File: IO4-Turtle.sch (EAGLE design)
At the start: 30 parts, among them CON1 RJ12/6, IC1 TC4428A, IC2 NE555S, Q1 NPN, X2 MSTBA5

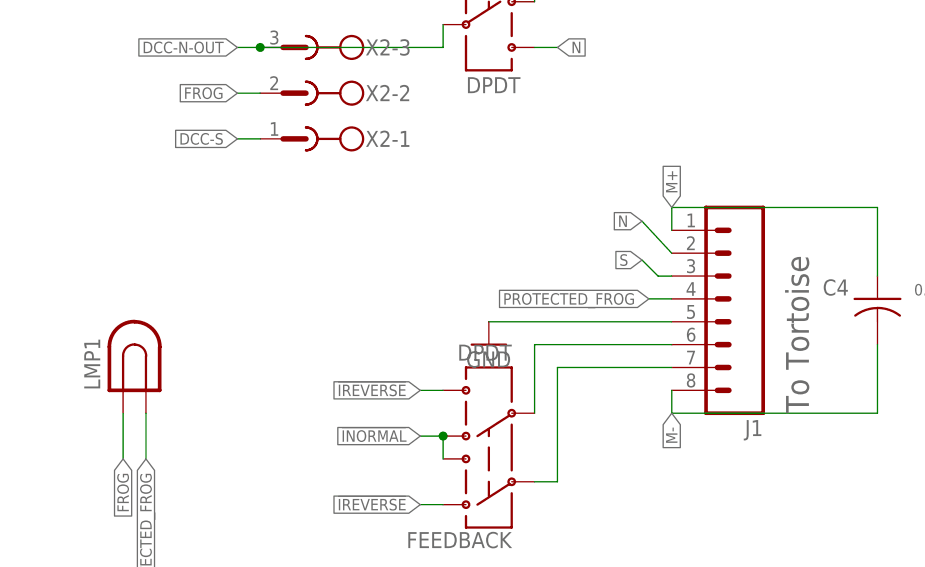
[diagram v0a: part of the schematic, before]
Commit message: added values for connectors
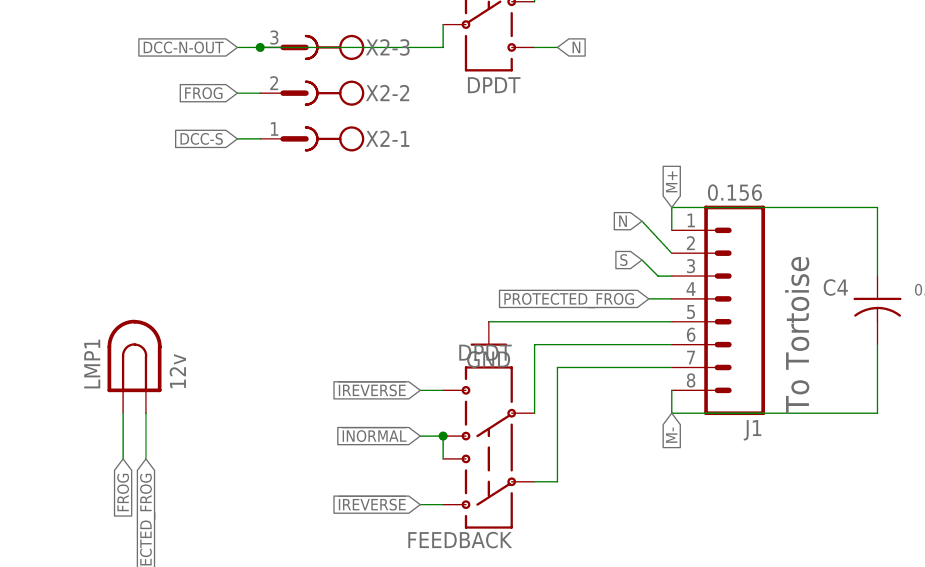
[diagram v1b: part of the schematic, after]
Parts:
- J1: value (none) -> 0.156
- LMP1: value (none) -> 12v
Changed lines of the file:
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@@
 <part name="P+4" library="SPCoast" deviceset="VCCIO" device=""/>
 <part name="P+5" library="SPCoast" deviceset="VCC" device=""/>
-<part name="LMP1" library="SPCoast" deviceset="LAMP" device="BULB"/>
-<part name="J1" library="SPCoast" deviceset="CONNECTOR-M08" device="1.56-F"/>
+<part name="LMP1" library="SPCoast" deviceset="LAMP" device="BULB" value="12v"/>
+<part name="J1" library="SPCoast" deviceset="CONNECTOR-M08" device="1.56-F" value="0.156"/>
 <part name="OSHW1" library="SPCoast" deviceset="DOC-OSHW-LOGO-" device="M"/>
 </parts>

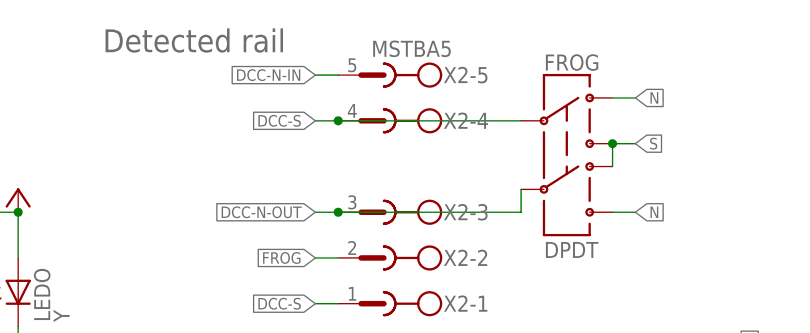
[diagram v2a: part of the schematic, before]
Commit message: normalized values
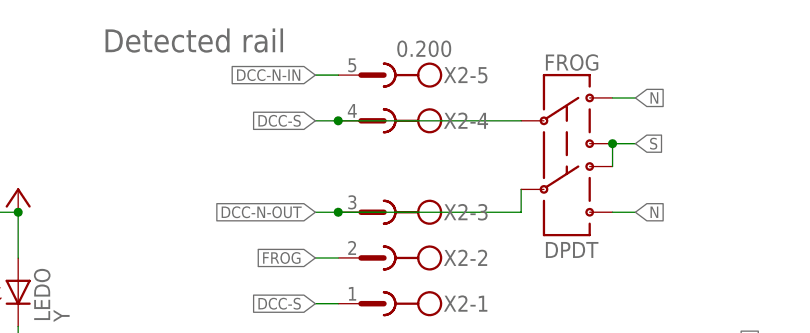
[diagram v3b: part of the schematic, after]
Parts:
- C1, C3: device SPCoast:CAP0805 -> SPCoast:CAP0603
- OSHW1: value DOC-OSHW-LOGO-M -> OSHW
- R1, R2, R3, R4, R5, R6, R7: device SPCoast:R0805-RES -> SPCoast:R0603-RES
- X2: value MSTBA5 -> 0.200
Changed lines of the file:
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@@
 <layer number="27" name="tValues" color="56" fill="1" visible="no" active="no"/>
 <layer number="28" name="bValues" color="7" fill="1" visible="no" active="no"/>
-<layer number="29" name="tStop" color="7" fill="3" visible="no" active="no"/>
+<layer number="29" name="tStop" color="32" fill="3" visible="no" active="no"/>
 <layer number="30" name="bStop" color="7" fill="6" visible="no" active="no"/>
 <layer number="31" name="tCream" color="7" fill="4" visible="no" active="no"/>
@@
 <layer number="46" name="Milling" color="35" fill="1" visible="no" active="no"/>
 <layer number="47" name="Measures" color="21" fill="1" visible="no" active="no"/>
-<layer number="48" name="Document" color="36" fill="1" visible="no" active="no"/>
+<layer number="48" name="Document" color="22" fill="1" visible="no" active="no"/>
 <layer number="49" name="Reference" color="48" fill="1" visible="no" active="no"/>
 <layer number="50" name="dxf" color="7" fill="1" visible="no" active="no"/>
-<layer number="51" name="tDocu" color="24" fill="1" visible="no" active="no"/>
-<layer number="52" name="bDocu" color="7" fill="1" visible="no" active="no"/>
+<layer number="51" name="tDocu" color="49" fill="1" visible="no" active="no"/>
+<layer number="52" name="bDocu" color="29" fill="1" visible="no" active="no"/>
 <layer number="53" name="tGND_GNDA" color="7" fill="9" visible="no" active="no"/>
 <layer number="54" name="bGND_GNDA" color="1" fill="9" visible="no" active="no"/>
@@
 <part name="GND2" library="SPCoast" deviceset="GND" device=""/>
 <part name="TR1" library="SPCoast" deviceset="PULSE-TRANSFORMER" device="PTH" value="CoilCraft"/>
-<part name="R7" library="SPCoast" deviceset="R*" device="0805-RES" value="10K"/>
-<part name="R5" library="SPCoast" deviceset="R*" device="0805-RES" value="1K0"/>
-<part name="C3" library="SPCoast" deviceset="CAP*" device="0805" value="2.2uf"/>
+<part name="R7" library="SPCoast" deviceset="R*" device="0603-RES" value="10K"/>
+<part name="R5" library="SPCoast" deviceset="R*" device="0603-RES" value="1K0"/>
+<part name="C3" library="SPCoast" deviceset="CAP*" device="0603" value="2.2uf"/>
 <part name="C2" library="SPCoast" deviceset="CAP-POL*" device="D" value="100uf"/>
 <part name="LEDO" library="SPCoast" deviceset="LED*" device="0603-LED" value="Y"/>
 <part name="GND4" library="SPCoast" deviceset="GND" device=""/>
 <part name="P+2" library="SPCoast" deviceset="VCC" device=""/>
-<part name="X2" library="SPCoast" deviceset="MSTBA5" device=""/>
+<part name="X2" library="SPCoast" deviceset="MSTBA5" device="" value="0.200"/>
 <part name="GND5" library="supply1" deviceset="GND" device=""/>
 <part name="LEDR" library="SPCoast" deviceset="LED*" device="0603-LED" value="R"/>
@@
 <part name="GND3" library="SPCoast" deviceset="GND" device=""/>
 <part name="P+6" library="SPCoast" deviceset="VCC" device=""/>
-<part name="R6" library="SPCoast" deviceset="R*" device="0805-RES" value="1M0"/>
+<part name="R6" library="SPCoast" deviceset="R*" device="0603-RES" value="1M0"/>
 <part name="GND6" library="SPCoast" deviceset="GND" device=""/>
 <part name="FROG" library="SPCoast" deviceset="SWITCH-DPDT" device="PTH-PB" value="DPDT"/>
 <part name="MOTOR" library="SPCoast" deviceset="SWITCH-DPDT" device="PTH-PB" value="DPDT"/>
 <part name="FEEDBACK" library="SPCoast" deviceset="SWITCH-DPDT" device="PTH-PB" value="DPDT"/>
-<part name="R4" library="SPCoast" deviceset="R*" device="0805-RES" value="2K0"/>
-<part name="R3" library="SPCoast" deviceset="R*" device="0805-RES" value="10k"/>
-<part name="R1" library="SPCoast" deviceset="R*" device="0805-RES" value="10k"/>
-<part name="R2" library="SPCoast" deviceset="R*" device="0805-RES" value="10k"/>
+<part name="R4" library="SPCoast" deviceset="R*" device="0603-RES" value="2K0"/>
+<part name="R3" library="SPCoast" deviceset="R*" device="0603-RES" value="10k"/>
+<part name="R1" library="SPCoast" deviceset="R*" device="0603-RES" value="10k"/>
+<part name="R2" library="SPCoast" deviceset="R*" device="0603-RES" value="10k"/>
 <part name="P+3" library="SPCoast" deviceset="VCCIO" device=""/>
 <part name="CON1" library="SPCoast" deviceset="CONNECTOR-RJ25" device="-43860-2-MOLEX" value="RJ12/6"/>
 <part name="VR1" library="SPCoast" deviceset="VREG-?-*" device="GOI" technology="5" value="LM1117-5"/>
 <part name="P+1" library="SPCoast" deviceset="VCCIO" device=""/>
-<part name="C1" library="SPCoast" deviceset="CAP*" device="0805" value="10uf"/>
+<part name="C1" library="SPCoast" deviceset="CAP*" device="0603" value="10uf"/>
 <part name="FID1" library="SPCoast" deviceset="FIDUCIAL" device=""/>
 <part name="FID2" library="SPCoast" deviceset="FIDUCIAL" device=""/>
@@
 <part name="LMP1" library="SPCoast" deviceset="LAMP" device="BULB" value="12v"/>
 <part name="J1" library="SPCoast" deviceset="CONNECTOR-M08" device="1.56-F" value="0.156"/>
-<part name="OSHW1" library="SPCoast" deviceset="DOC-OSHW-LOGO-" device="M"/>
+<part name="OSHW1" library="SPCoast" deviceset="DOC-OSHW-LOGO-" device="M" value="OSHW"/>
 </parts>
 <sheets>
